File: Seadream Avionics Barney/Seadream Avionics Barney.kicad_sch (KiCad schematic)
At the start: 41 parts, among them J1 B2B-PH-K-S(LF)(SN), J2 C393939, J3 B2B-PH-K-S(LF)(SN), SW1 SSSS810701, U1 BMP280, U2 ESP32-S3-MINI-1U-N8, U3 LSM6DSO32TR, U4 LD1117S33TR, U5 SHT40-AD1B-R3, U6 LD39200PU33R, U7 MAX98357AETE_T

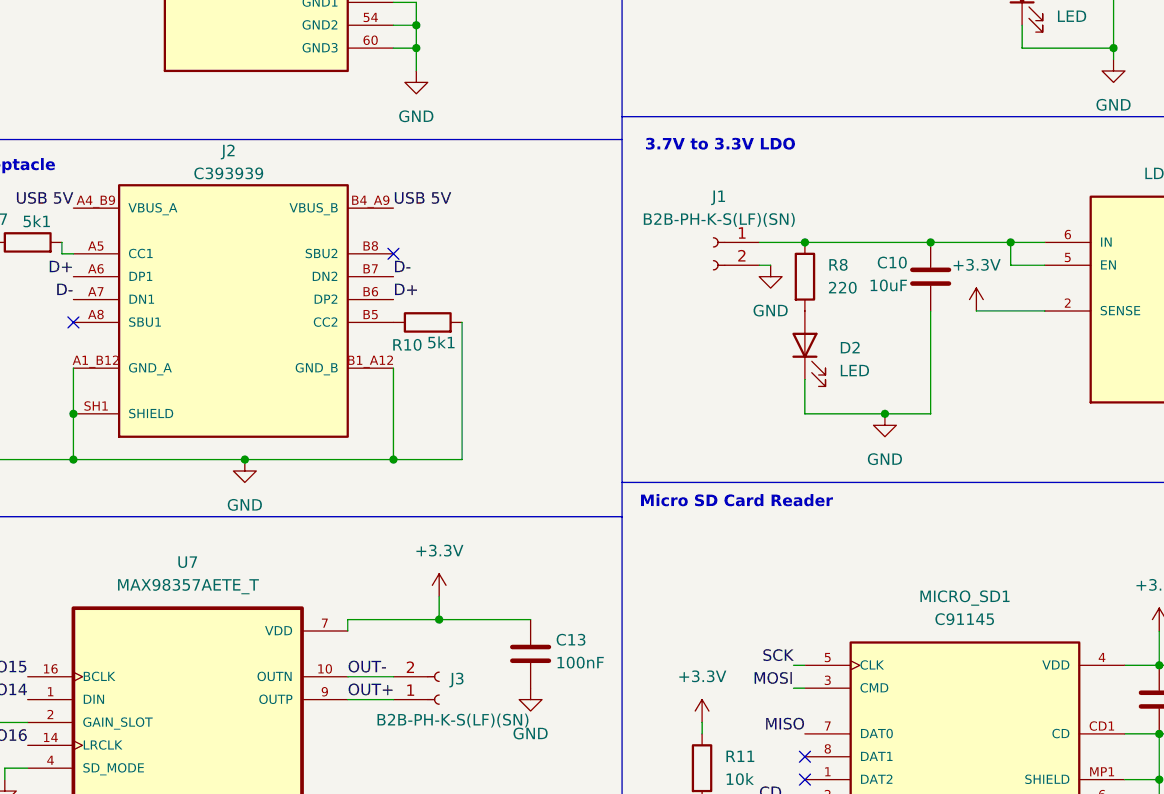
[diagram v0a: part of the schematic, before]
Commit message: Added more info to BOM for JLCPCB PCBA
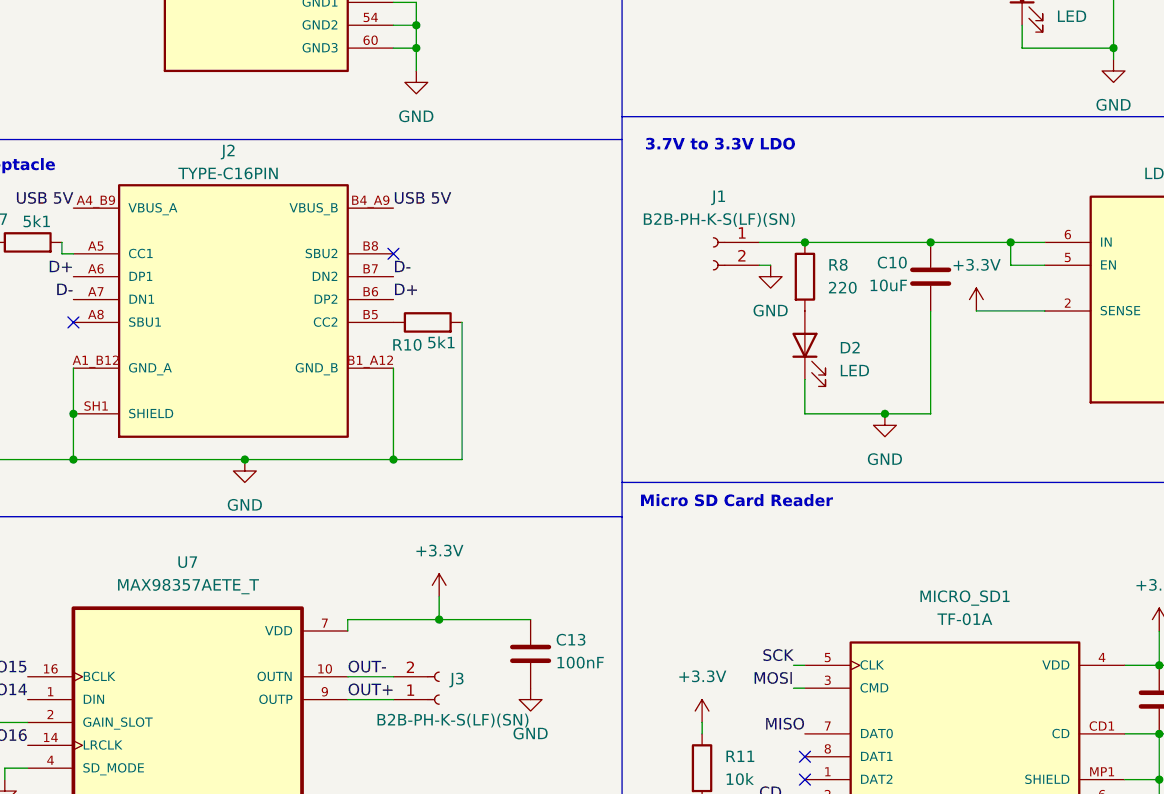
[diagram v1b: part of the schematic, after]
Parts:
- C1, C12, C13, C14, C3, C4, C5, C6, C7: Part NO. (none) -> C1525
- C10, C2, C8, C9: Part NO. (none) -> C19702
- C11: Part NO. (none) -> C45783
- C15: Part NO. (none) -> C52923
- D1, D2, D3: Part NO. (none) -> C84256
- J1, J3: Part NO. (none) -> C131337
- J2: value C393939 -> TYPE-C16PIN; footprint TYPE-C_16PIN_2MD__073_:SHOUHAN_TYPE-C_16PIN_2MD__073_ -> 2FOOTPRINTS:SHOUHAN_TYPE-C_16PIN_2MD__073_; Part NO. (none) -> C393939
- MICRO_SD1: value C91145 -> TF-01A; Part NO. (none) -> C91145
- R1, R11, R2: Part NO. (none) -> C25531
- R10, R7: Part NO. (none) -> C25905
- R3, R4: Part NO. (none) -> C25900
- R5: Part NO. (none) -> C23138
- R8, R9: Part NO. (none) -> C22962
- S1: Part NO. (none) -> C72443
- SW1: Part NO. (none) -> C97433
- U1: Part NO. (none) -> C83291
- U2: Part NO. (none) -> C2980299
- U3: Part NO. (none) -> C1864162
- U4: Part NO. (none) -> C86781
- U5: Part NO. (none) -> C2848306
- U6: Part NO. (none) -> C222192
- U7: Part NO. (none) -> C910544
